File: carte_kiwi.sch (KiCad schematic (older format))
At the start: 35 parts, among them IC1 MCP2562, P2 Serial Wire, P3 UART, U1 STM32F303K8, U4 LD1117S33TR

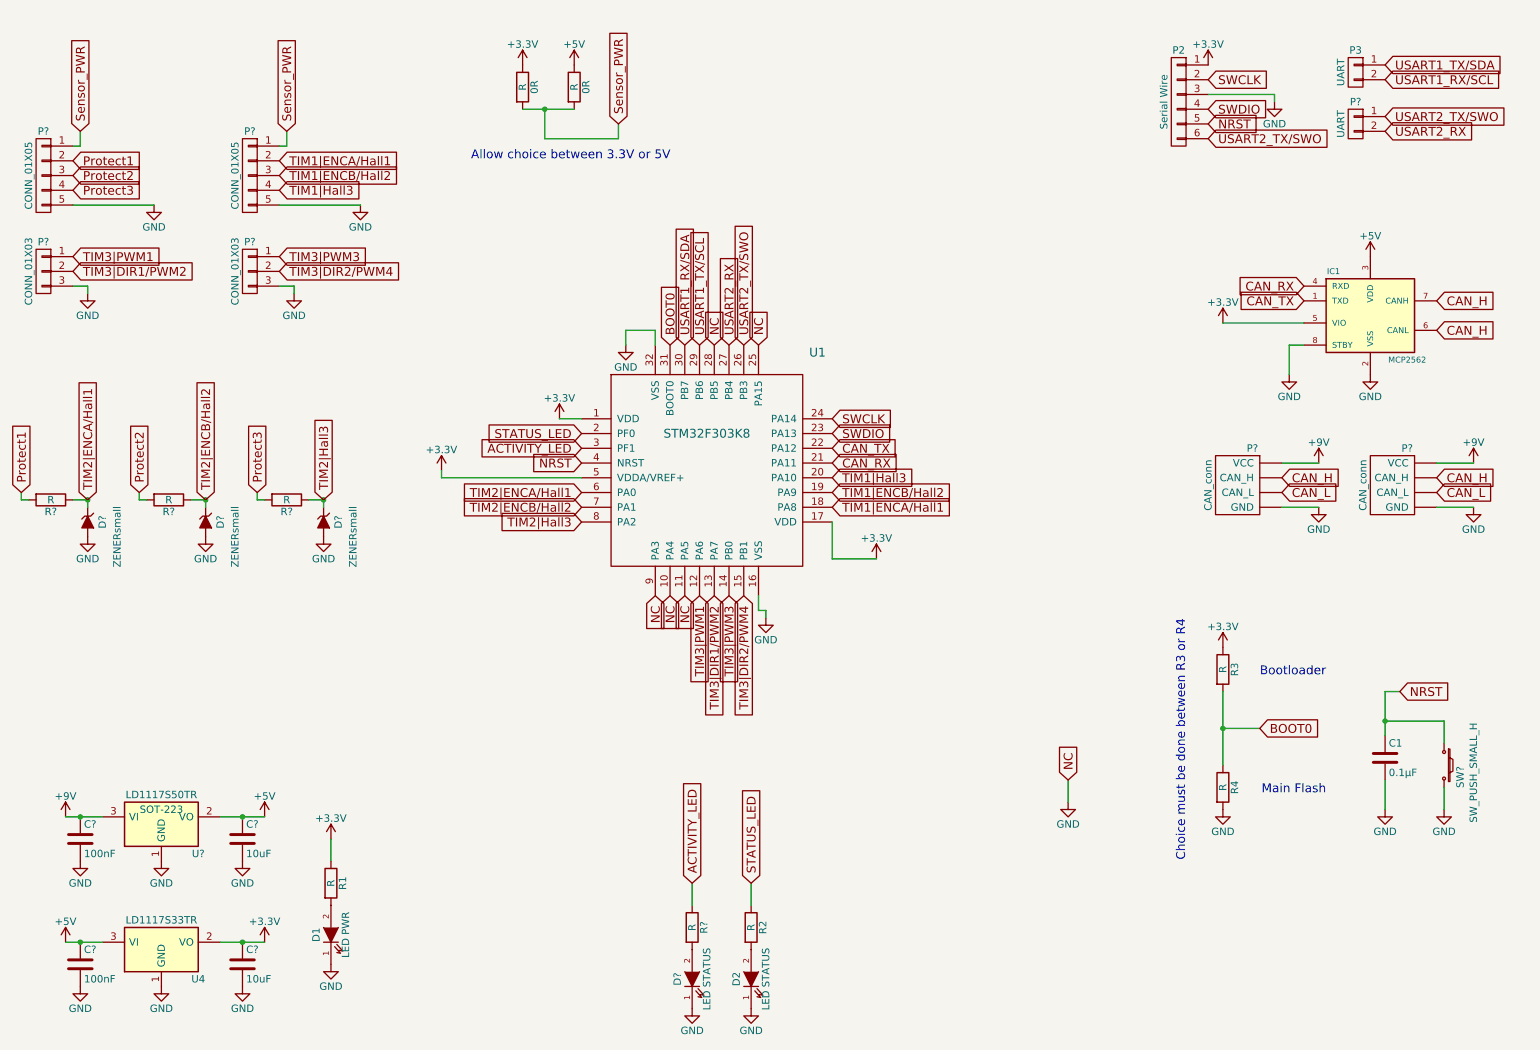
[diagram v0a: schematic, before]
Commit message: association emprunte + correction erreurs
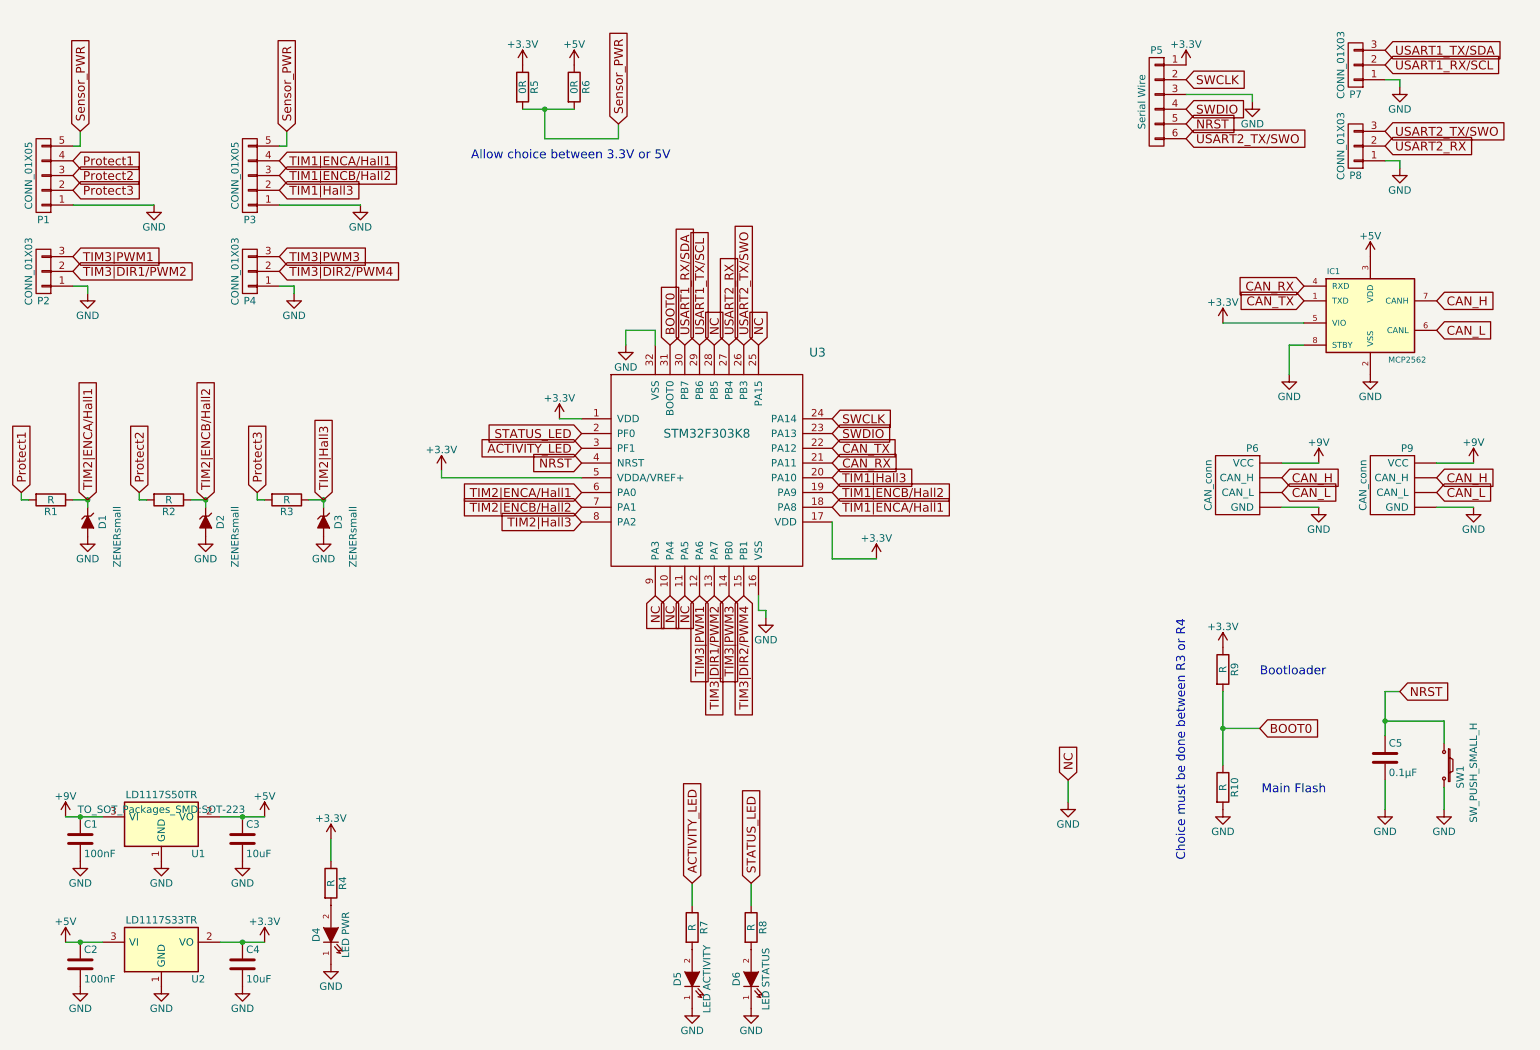
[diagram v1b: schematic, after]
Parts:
- removed P3, P?: UART, Pin_Headers:Pin_Header_Straight_1x02, symbol CONN_01X02
- added P7, P8: CONN_01X03, Pin_Headers:Pin_Header_Straight_1x03, symbol CONN_01X03
- C1, C2, C3, C4: renamed from C?; footprint (none) -> Capacitors_SMD:C_0805_HandSoldering
- D1, D2, D3: renamed from D?; footprint (none) -> Diodes_SMD:SOD-123
- D5: renamed from D?; value LED STATUS -> LED ACTIVITY
- P1, P3: renamed from P?; footprint (none) -> Connectors_JST:JST_XH_B05B-XH-A_05x2.50mm_Straight
- P2, P4: renamed from P?; footprint (none) -> Pin_Headers:Pin_Header_Straight_1x03
- P6, P9: renamed from P?; footprint (none) -> Connectors_JST:JST_XH_B04B-XH-A_04x2.50mm_Straight
- R1, R2, R3: renamed from R?; footprint (none) -> Resistors_SMD:R_0805_HandSoldering
- R5, R6: renamed from 0R; value R -> 0R; footprint (none) -> Resistors_SMD:R_0805_HandSoldering
- SW1: renamed from SW?; footprint (none) -> Buttons_Switches_SMD:SW_SPST_EVQPE1
- U1: renamed from U?; footprint SOT-223 -> TO_SOT_Packages_SMD:SOT-223
- U2: renamed from U4; footprint (none) -> TO_SOT_Packages_SMD:SOT-223
- gave numbers to parts that had none: 1
- renumbered C1 to C5, D1 to D4, D2 to D6, P2 to P5, R4 to R10, R1 to R4, R2 to R8, R3 to R9, U1 to U3
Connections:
- net CAN_H: no longer IC1.6 (CANL)
- net CAN_L: now also IC1.6 (CANL)
- net GND: now also P1.1 (P1), P2.1 (P1), P3.1 (P1), P4.1 (P1), P7.1 (P1), P8.1 (P1); no longer P1.5 (P5), P2.3 (P3), P3.5 (P5), P4.3 (P3)
- net Protect1: now also P1.4 (P4); no longer P1.2 (P2)
- net Protect3: now also P1.2 (P2); no longer P1.4 (P4)
- net Sensor_PWR: now also P1.5 (P5), P3.5 (P5); no longer P1.1 (P1), P3.1 (P1)
- net TIM1|ENCA/Hall1: now also P3.4 (P4); no longer P3.2 (P2)
- net TIM1|Hall3: now also P3.2 (P2); no longer P3.4 (P4)
- net TIM3|PWM1: now also P2.3 (P3); no longer P2.1 (P1)
- net TIM3|PWM3: now also P4.3 (P3); no longer P4.1 (P1)
- net USART1_RX/SCL: now also P7.2 (P2)
- net USART1_TX/SDA: now also P7.3 (P3)
- net USART2_RX: now also P8.2 (P2)
- net USART2_TX/SWO: now also P8.3 (P3)
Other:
- moved on the sheet: P5

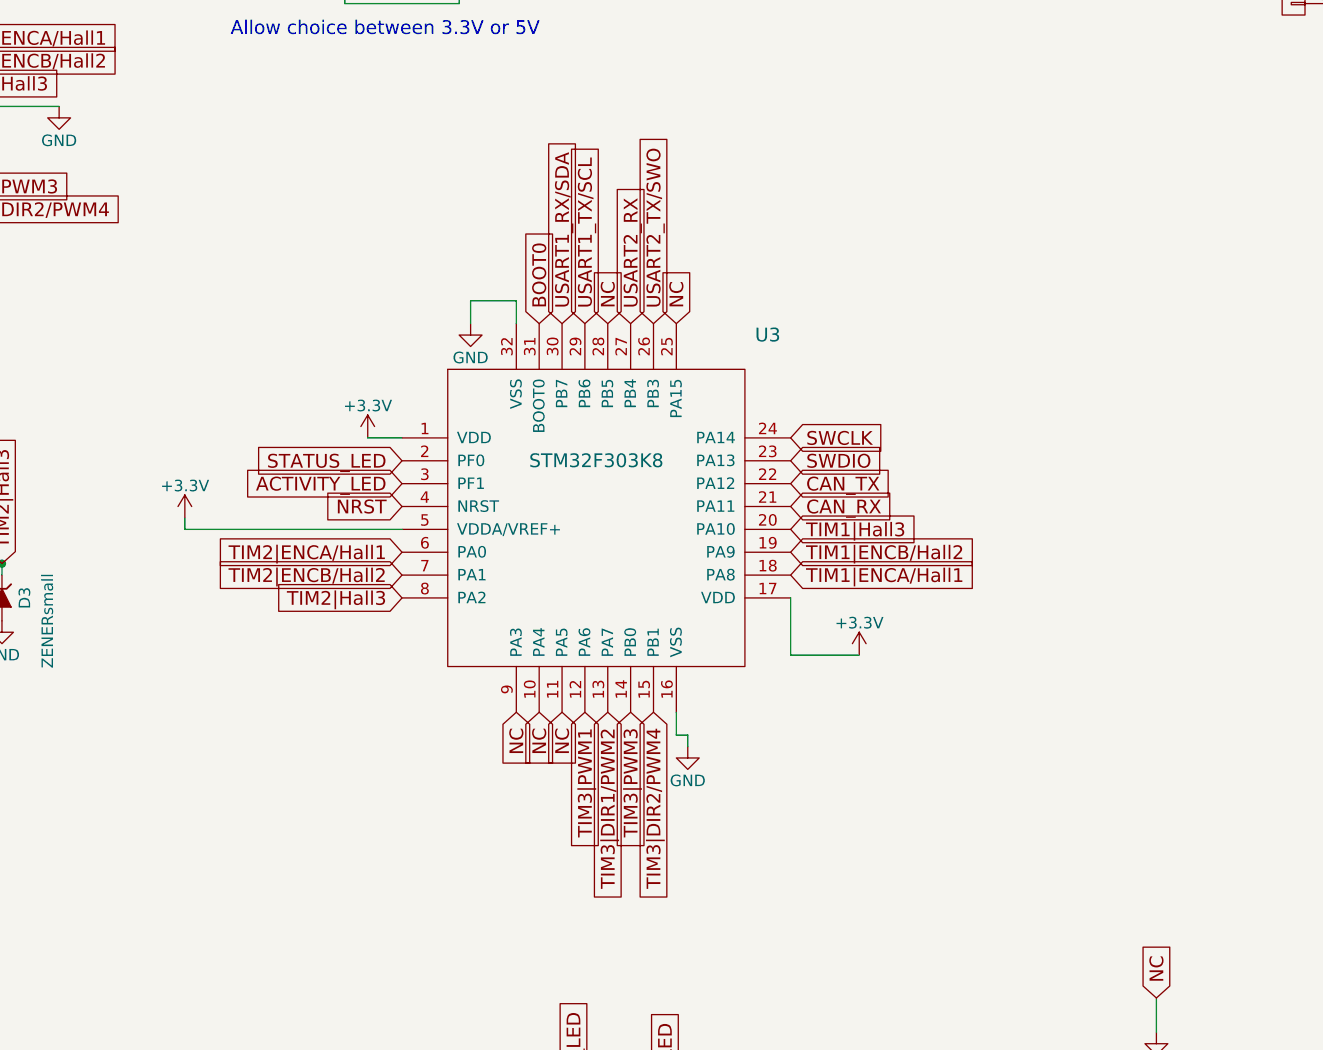
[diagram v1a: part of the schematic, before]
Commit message: ajoute capa découplage
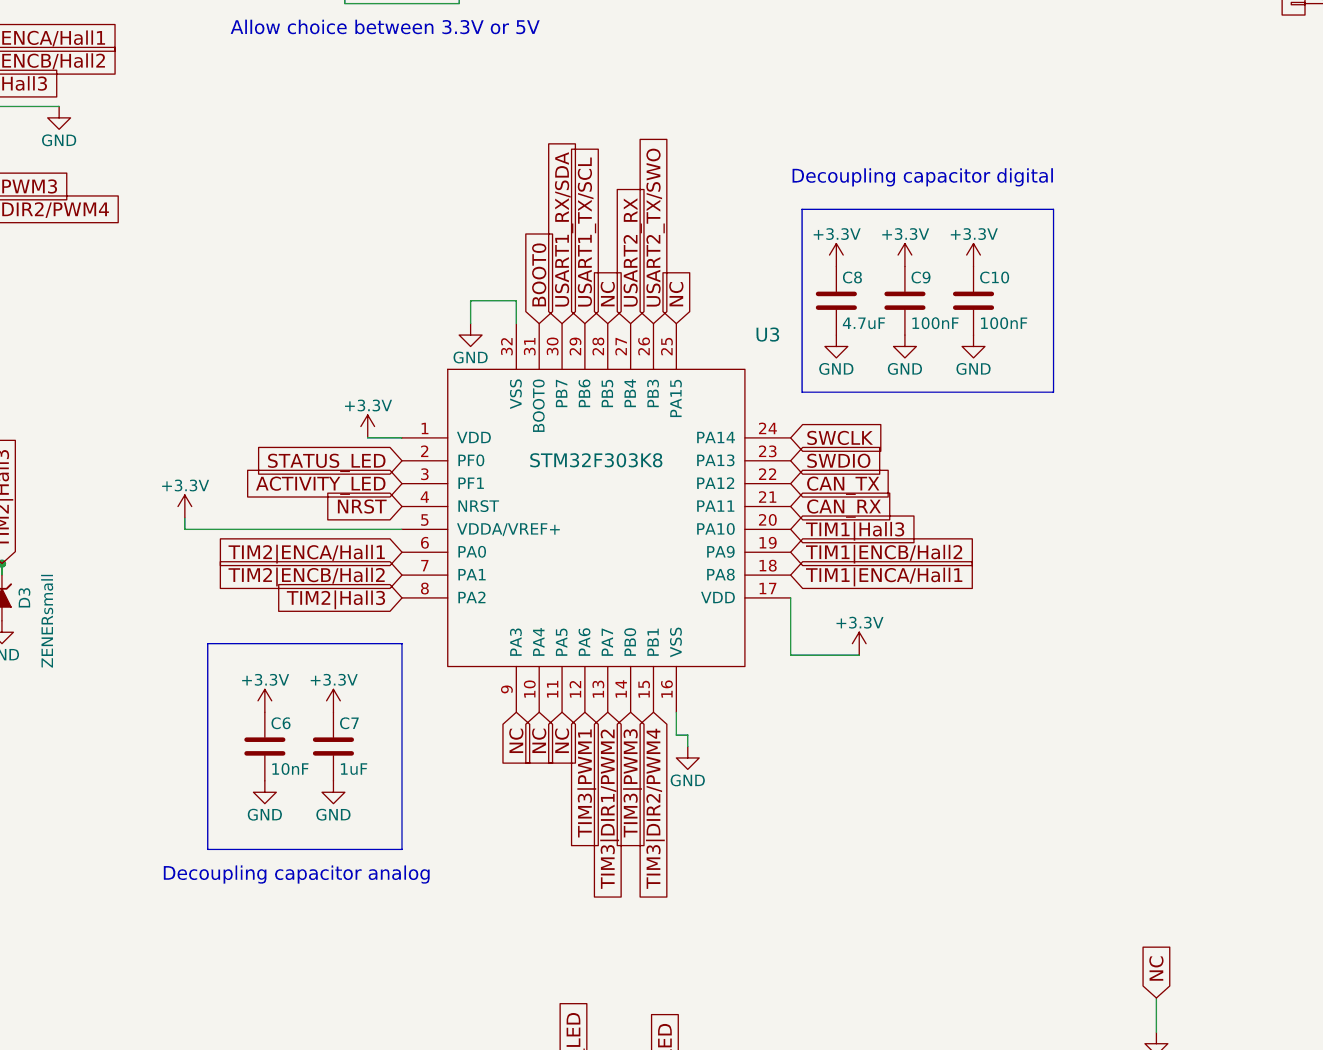
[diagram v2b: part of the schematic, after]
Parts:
- added C10, C9: 100nF, Capacitors_SMD:C_0805_HandSoldering, symbol C
- added C6: 10nF, Capacitors_SMD:C_0805_HandSoldering, symbol C
- added C7: 1uF, Capacitors_SMD:C_0805_HandSoldering, symbol C
- added C8: 4.7uF, Capacitors_SMD:C_0805_HandSoldering, symbol C
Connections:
- net +3V3: now also C10.1, C6.1, C7.1, C8.1, C9.1
- net GND: now also C10.2, C6.2, C7.2, C8.2, C9.2
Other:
- note added: "Decoupling capacitor analog"
- note added: "Decoupling capacitor digital"

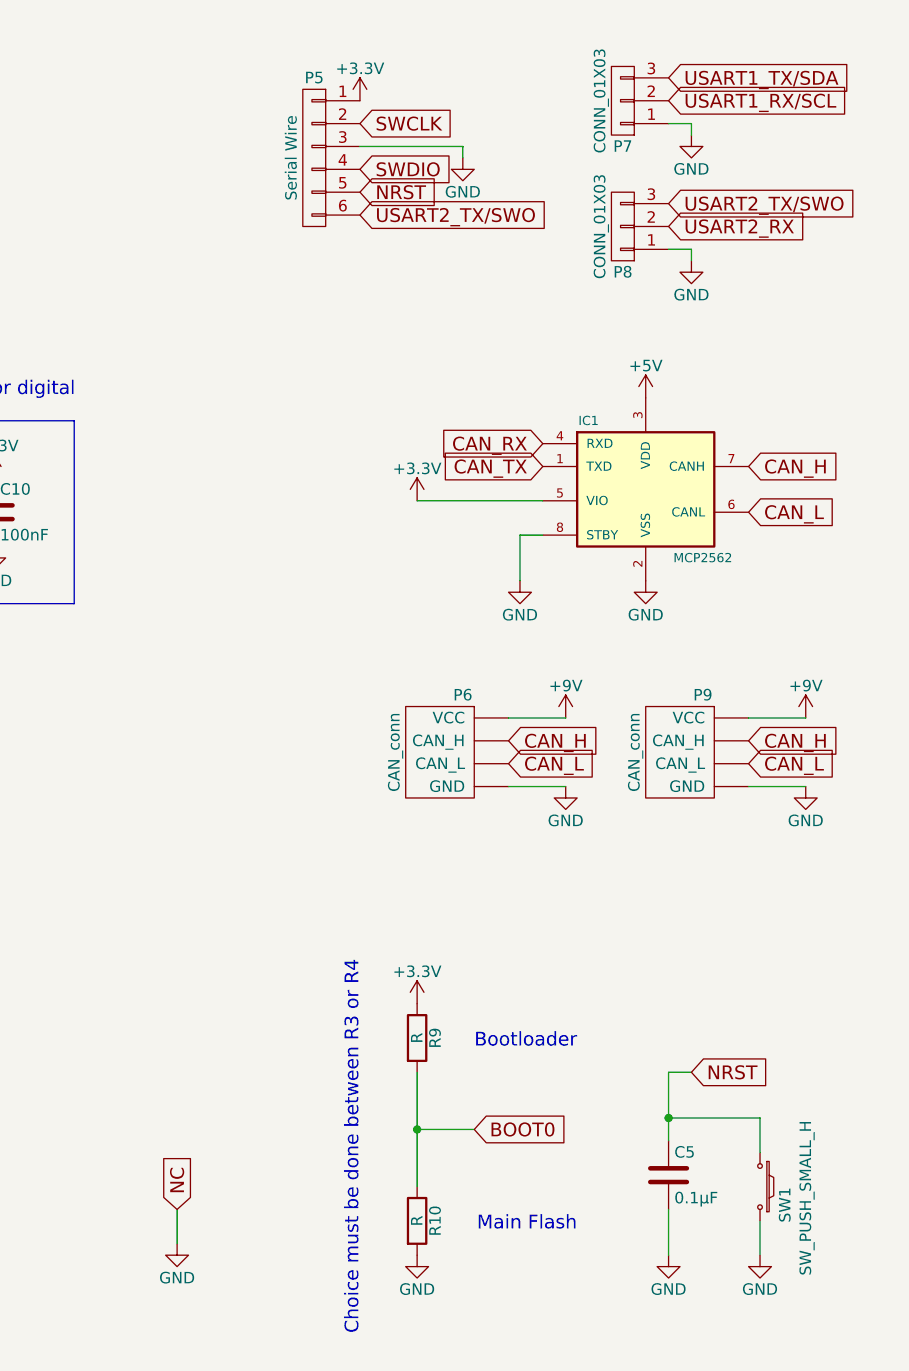
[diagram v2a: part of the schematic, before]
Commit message: correction inversion SCL et SDA + évite renomage systématique des nets GND en NC
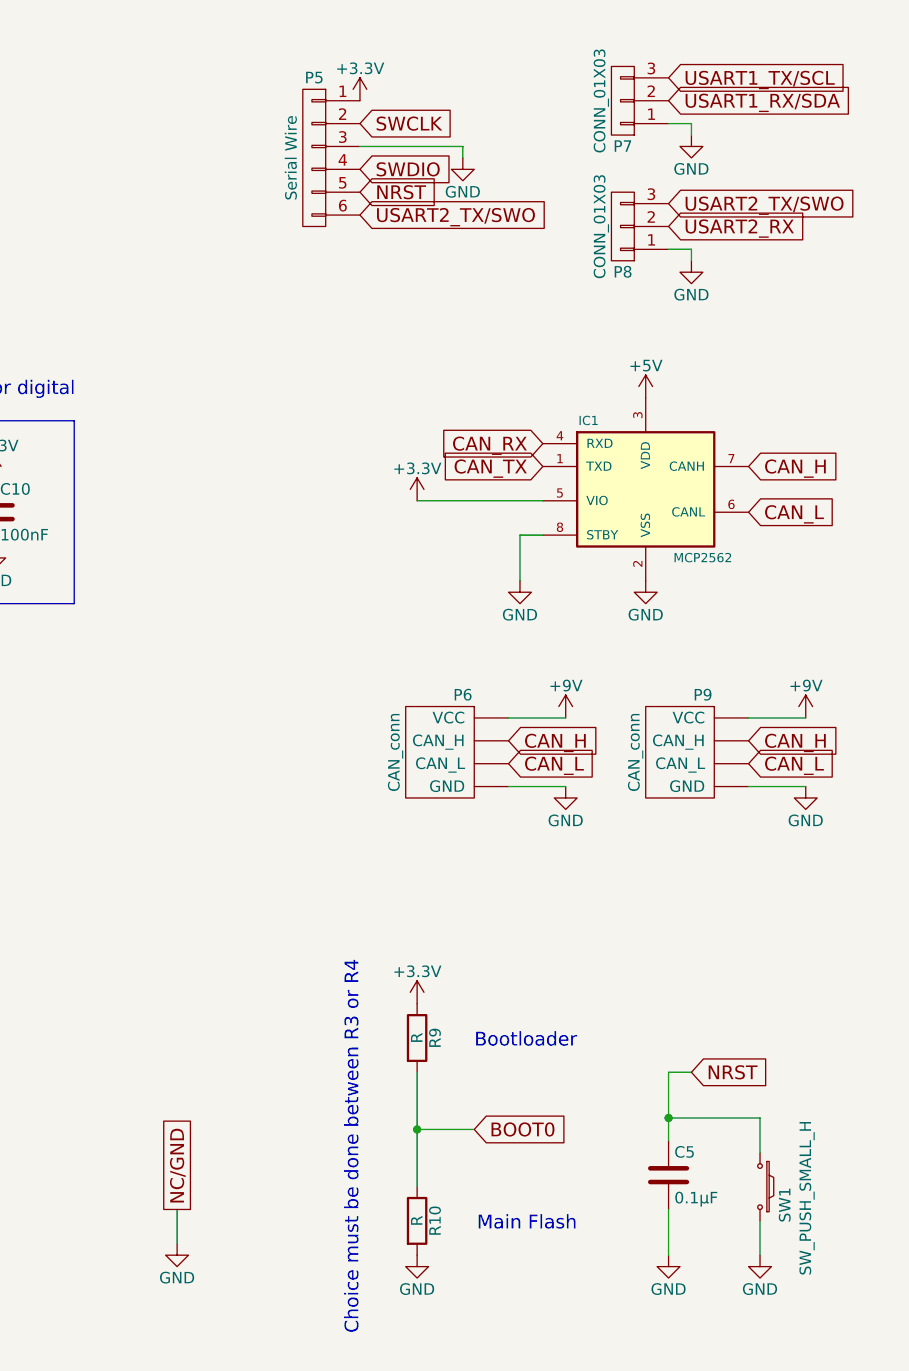
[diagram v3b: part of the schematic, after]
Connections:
- net USART1_RX/SCL is gone; now on net USART1_RX/SDA: P7.2 (P2)
- net USART1_TX/SDA is gone; now on net USART1_TX/SCL: P7.3 (P3)
- net GND: no longer U3.10 (PA4), U3.11 (PA5), U3.25 (PA15), U3.28 (PB5), U3.9 (PA3)
- new net NC: U3.10 (PA4), U3.11 (PA5), U3.25 (PA15), U3.28 (PB5), U3.9 (PA3)
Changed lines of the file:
@@
 $EndComp
 Text GLabel 10100 800  2    60   Input ~ 0
-USART1_TX/SDA
+USART1_TX/SCL
 Text GLabel 10100 900  2    60   Input ~ 0
-USART1_RX/SCL
+USART1_RX/SDA
 Text GLabel 4650 3400 0    60   Input ~ 0
 STATUS_LED
@@
 Text GLabel 5350 4500 3    60   Input ~ 0
 NC
-Text GLabel 7950 5750 1    60   Input ~ 0
-NC
+Text GLabel 7950 5750 1    60   UnSpc ~ 0
+NC/GND
 $Comp
 L GND #PWR043
